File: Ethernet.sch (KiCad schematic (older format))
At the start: 2 parts

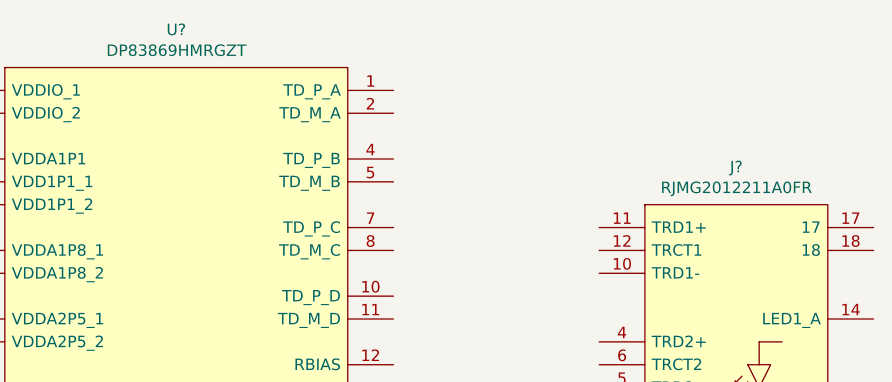
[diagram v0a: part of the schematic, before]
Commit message: Completeed the FPGA_Power sheet Created PCB
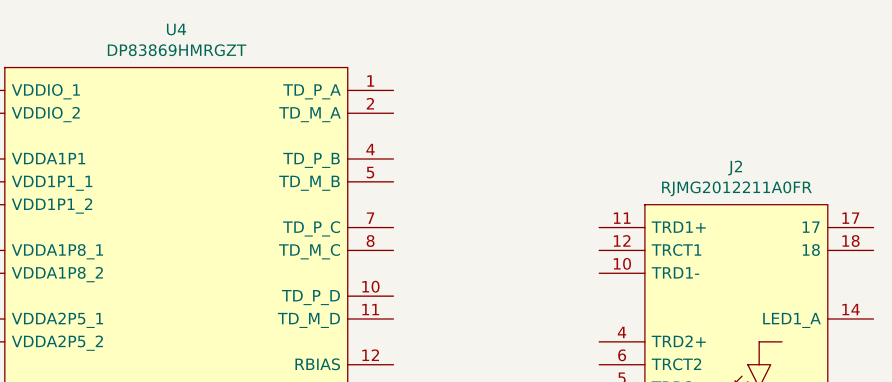
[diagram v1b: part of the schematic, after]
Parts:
- gave numbers to parts that had none: 2
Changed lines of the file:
@@
 $EndDescr
 $Comp
-L GM_Connectors:RJMG2012211A0FR J?
+L GM_Connectors:RJMG2012211A0FR J2
 U 1 1 601C9357
 P 7900 2300
-F 0 "J?" H 8300 2465 50  0000 C CNN
+F 0 "J2" H 8300 2465 50  0000 C CNN
 F 1 "RJMG2012211A0FR" H 8300 2374 50  0000 C CNN
 F 2 "Connector_RJ:RJ45_Amphenol_RJMG2012211A0FR" H 9650 2000 50  0001 L CNN
@@
 $EndComp
 $Comp
-L GM_Interface_IC:DP83869HMRGZT U?
+L GM_Interface_IC:DP83869HMRGZT U4
 U 1 1 601CAF41
 P 5100 1700
-F 0 "U?" H 5850 1865 50  0000 C CNN
+F 0 "U4" H 5850 1865 50  0000 C CNN
 F 1 "DP83869HMRGZT" H 5850 1774 50  0000 C CNN
 F 2 "QFN50P700X700X100-49N-D" H 8650 800 50  0001 L CNN
